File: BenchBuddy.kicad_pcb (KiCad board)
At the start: 4 copper layers, 152.4 x 63.5 mm, 122 parts, among them K1 1461069-5, P1 24 Pin MiniFit JR, P2 CONN_3X2, P3 CONN_2, P4 12 Pin Terminal Block, P5 3 Pin TB, Q1 2N3904, Q2 DMN65D8L-7, Q3 AOD476, Q4 AOD476, SW1 OS102011MA1QN1, U1 LTV-816S, U11 LM317, U12 ARDUINOPINS, U2 MCP3901, U20 OPA4170, U3 LMT84, U4 MCP4801, U6 LM317, U7 LM337T, U8 LM337T

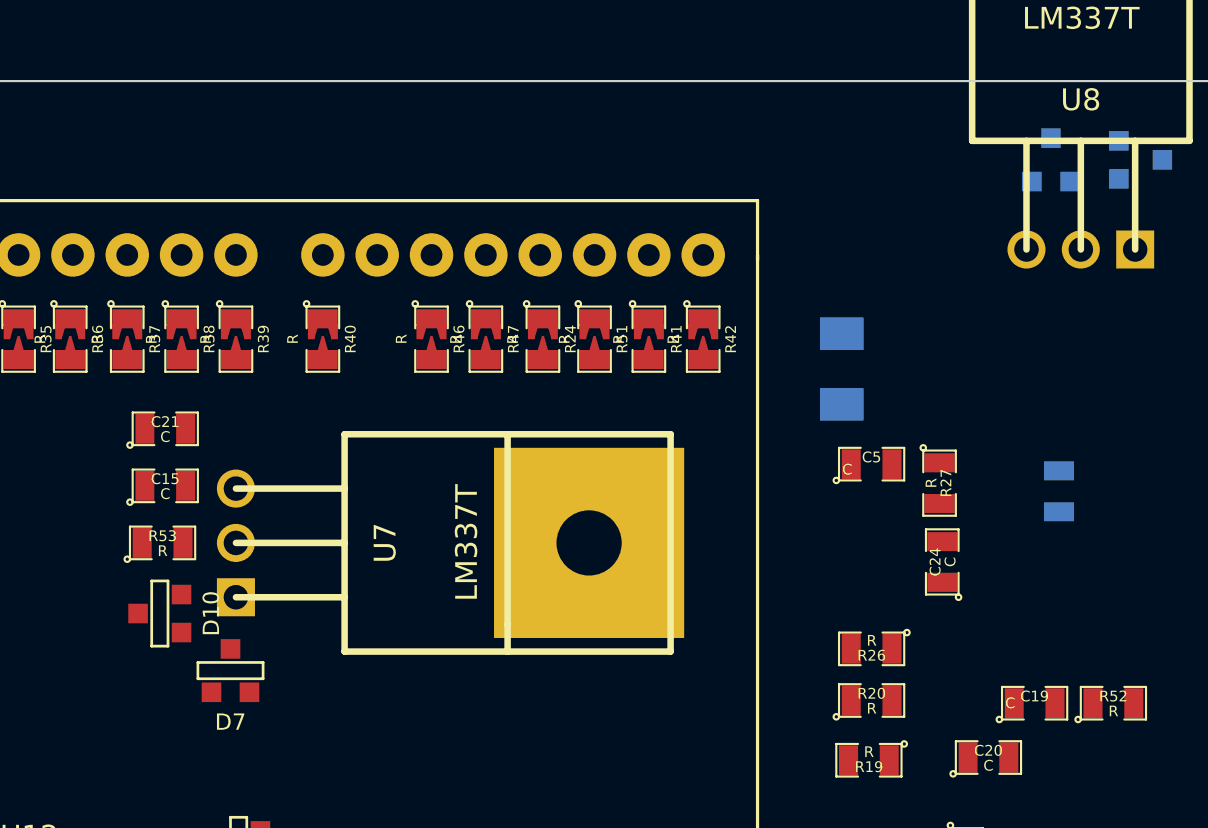
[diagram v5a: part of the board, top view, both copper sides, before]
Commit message: Power Modification Module - Correct Diode Polarity
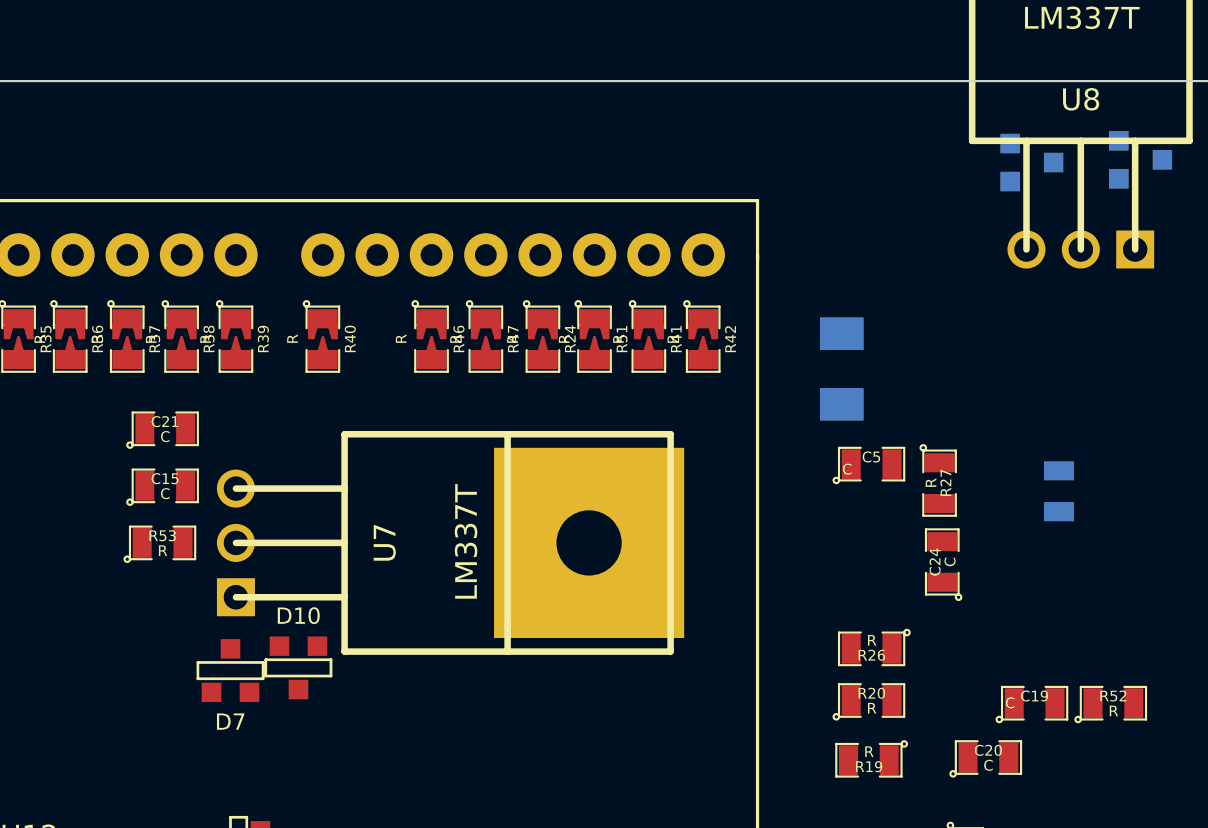
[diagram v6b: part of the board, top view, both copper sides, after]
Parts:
- moved D10 6.96 mm to (186.2, 133.1), turned to 0 degrees
- moved D12 0.90 mm to (220.5, 109.5), turned to 270 degrees
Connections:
- D10 pad 1: FE_V- -> -12V
- D10 pad 2: -12V -> FE_V-
- D12 pad 1: /PowerAdjustmentMonitor/V-_ADJ -> -12V
- D12 pad 2: -12V -> /PowerAdjustmentMonitor/V-_ADJ
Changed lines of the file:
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@@
   (general
     (links 343)
-    (no_connects 299)
+    (no_connects 298)
     (area 139.014999 105.613999 291.515001 169.214001)
     (thickness 1.6)
@@
   )
   (module SOT23-DIODE (layer F.Cu)
-    (at 179.705 130.556 270)
+    (at 186.182 133.096)
     (descr "Module CMS SOT23 Transistore EBC")
     (tags "CMS SOT")
     (attr smd)
-    (fp_text reference D10 (at 0 -2.413 270) (layer F.SilkS)
+    (fp_text reference D10 (at 0 -2.413) (layer F.SilkS)
       (effects (font (size 0.762 0.762) (thickness 0.1905)))
     )
-    (fp_text value MMBD914-7-F (at 0 0 270) (layer F.SilkS) hide
+    (fp_text value MMBD914-7-F (at 0 0) (layer F.SilkS) hide
       (effects (font (size 0.762 0.762) (thickness 0.2032)))
     )
@@
     (fp_line (start 1.524 0.381) (end -1.524 0.381) (layer F.SilkS) (width 0.127))
     (fp_line (start -1.524 0.381) (end -1.524 -0.381) (layer F.SilkS) (width 0.127))
-    (pad 3 smd rect (at -0.889 -1.016 270) (size 0.9144 0.9144)
+    (pad 3 smd rect (at -0.889 -1.016) (size 0.9144 0.9144)
       (layers F.Cu F.Paste F.Mask)
     )
-    (pad 1 smd rect (at 0.889 -1.016 270) (size 0.9144 0.9144)
+    (pad 1 smd rect (at 0.889 -1.016) (size 0.9144 0.9144)
       (layers F.Cu F.Paste F.Mask)
-      (net 41 FE_V-)
+      (net 8 -12V)
     )
-    (pad 2 smd rect (at 0 1.016 270) (size 0.9144 0.9144)
+    (pad 2 smd rect (at 0 1.016) (size 0.9144 0.9144)
       (layers F.Cu F.Paste F.Mask)
-      (net 8 -12V)
+      (net 41 FE_V-)
     )
     (model smd/cms_sot23.wrl
@@
   )
   (module SOT23-DIODE (layer B.Cu)
-    (at 221.361 109.347)
+    (at 220.472 109.474 270)
     (descr "Module CMS SOT23 Transistore EBC")
     (tags "CMS SOT")
     (attr smd)
-    (fp_text reference D12 (at 0 2.413) (layer B.SilkS)
+    (fp_text reference D12 (at 0 2.413 270) (layer B.SilkS)
       (effects (font (size 0.762 0.762) (thickness 0.1905)) (justify mirror))
     )
-    (fp_text value MMBD914-7-F (at 0 0) (layer B.SilkS) hide
+    (fp_text value MMBD914-7-F (at 0 0 270) (layer B.SilkS) hide
       (effects (font (size 0.762 0.762) (thickness 0.2032)) (justify mirror))
     )
@@
     (fp_line (start 1.524 -0.381) (end -1.524 -0.381) (layer B.SilkS) (width 0.127))
     (fp_line (start -1.524 -0.381) (end -1.524 0.381) (layer B.SilkS) (width 0.127))
-    (pad 3 smd rect (at -0.889 1.016) (size 0.9144 0.9144)
+    (pad 3 smd rect (at -0.889 1.016 270) (size 0.9144 0.9144)
       (layers B.Cu B.Paste B.Mask)
     )
-    (pad 1 smd rect (at 0.889 1.016) (size 0.9144 0.9144)
+    (pad 1 smd rect (at 0.889 1.016 270) (size 0.9144 0.9144)
       (layers B.Cu B.Paste B.Mask)
-      (net 32 /PowerAdjustmentMonitor/V-_ADJ)
+      (net 8 -12V)
     )
-    (pad 2 smd rect (at 0 -1.016) (size 0.9144 0.9144)
+    (pad 2 smd rect (at 0 -1.016 270) (size 0.9144 0.9144)
       (layers B.Cu B.Paste B.Mask)
-      (net 8 -12V)
+      (net 32 /PowerAdjustmentMonitor/V-_ADJ)
     )
     (model smd/cms_sot23.wrl
